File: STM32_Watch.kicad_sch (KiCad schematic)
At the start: 44 parts, among them SW1 SW_Push, SW2 SW_Push, U1 STM32L031K6Ux, U2 LSM6DS3, X1 32.768k

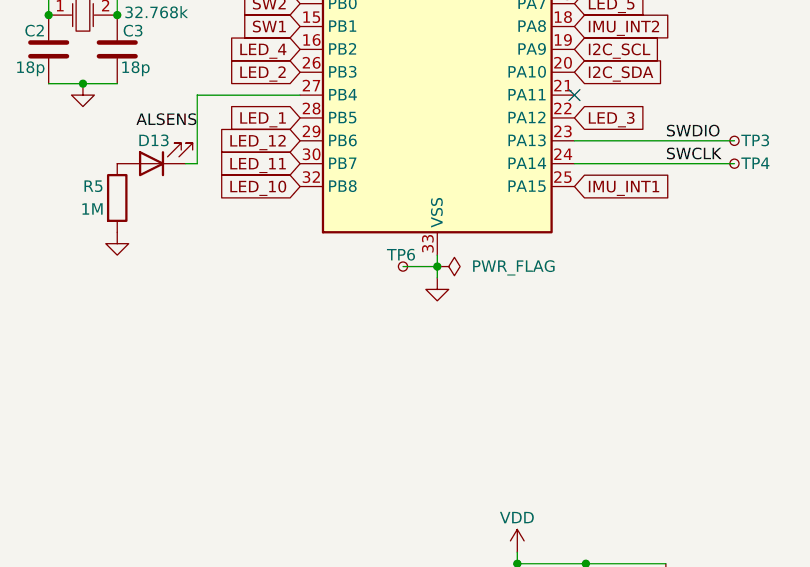
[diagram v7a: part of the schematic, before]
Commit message: Added GND TP & BOM file
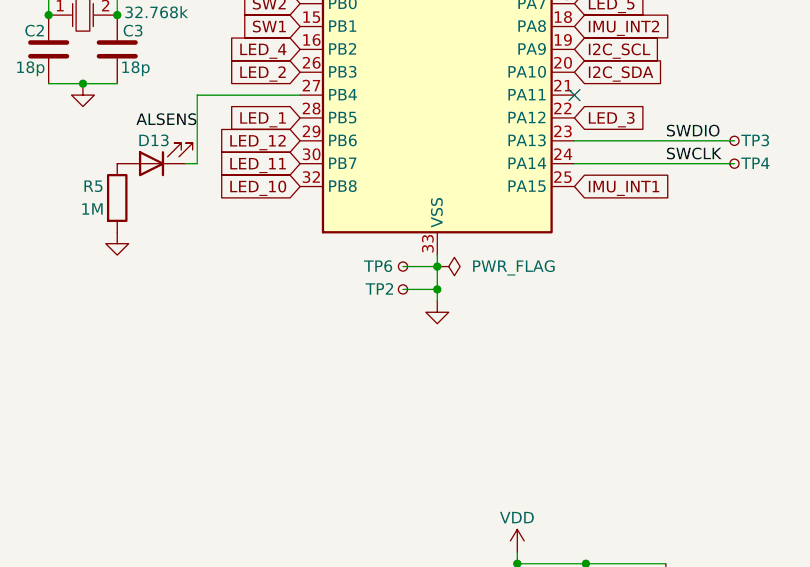
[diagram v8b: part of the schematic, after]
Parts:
- added TP2: TestPoint_Small, TestPoint:TestPoint_Pad_D1.5mm, symbol Connector:TestPoint_Small
- C7: LCSC C15850 -> C32635
- U2: LCSC C967633 -> C94048
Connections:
- net GND: now also TP2.1
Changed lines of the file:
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@@
 	)
 	(junction
+		(at 92.71 102.87)
+		(diameter 0)
+		(color 0 0 0 0)
+	)
+	(junction
 		(at 92.71 34.29)
 		(diameter 0)
@@
 	(wire
 		(pts
-			(xy 92.71 101.6) (xy 92.71 100.33)
+			(xy 88.9 102.87) (xy 92.71 102.87)
+		)
+		(stroke
+			(width 0)
+			(type default)
+		)
+	)
+	(wire
+		(pts
+			(xy 92.71 104.14) (xy 92.71 102.87)
 		)
 		(stroke
@@
 	(wire
 		(pts
+			(xy 92.71 102.87) (xy 92.71 100.33)
+		)
+		(stroke
+			(width 0)
+			(type default)
+		)
+	)
+	(wire
+		(pts
 			(xy 59.69 162.56) (xy 86.36 162.56)
 		)
@@
 	(symbol
 		(lib_id "power:GND")
-		(at 92.71 101.6 0)
+		(at 92.71 104.14 0)
 		(unit 1)
 		(exclude_from_sim no)
@@
 		(fields_autoplaced yes)
 		(property "Reference" "#PWR01"
-			(at 92.71 107.95 0)
+			(at 92.71 110.49 0)
 			(effects
 				(font
@@
 		)
 		(property "Value" "GND"
-			(at 92.71 106.68 0)
+			(at 92.71 109.22 0)
 			(effects
 				(font
@@
 		)
 		(property "Footprint" ""
-			(at 92.71 101.6 0)
+			(at 92.71 104.14 0)
 			(effects
 				(font
@@
 		)
 		(property "Datasheet" ""
-			(at 92.71 101.6 0)
+			(at 92.71 104.14 0)
 			(effects
 				(font
@@
 		)
 		(property "Description" "Power symbol creates a global label with name \"GND\" , ground"
-			(at 92.71 101.6 0)
+			(at 92.71 104.14 0)
 			(effects
 				(font
@@
 	)
 	(symbol
+		(lib_id "Connector:TestPoint_Small")
+		(at 88.9 102.87 90)
+		(unit 1)
+		(exclude_from_sim no)
+		(in_bom yes)
+		(on_board yes)
+		(dnp no)
+		(property "Reference" "TP2"
+			(at 86.36 102.87 90)
+			(effects
+				(font
+					(size 1.27 1.27)
+				)
+			)
+		)
+		(property "Value" "TestPoint_Small"
+			(at 88.9 100.33 90)
+			(effects
+				(font
+					(size 1.27 1.27)
+				)
+				(hide yes)
+			)
+		)
+		(property "Footprint" "TestPoint:TestPoint_Pad_D1.5mm"
+			(at 88.9 97.79 0)
+			(effects
+				(font
+					(size 1.27 1.27)
+				)
+				(hide yes)
+			)
+		)
+		(property "Datasheet" "~"
+			(at 88.9 97.79 0)
+			(effects
+				(font
+					(size 1.27 1.27)
+				)
+				(hide yes)
+			)
+		)
+		(property "Description" "test point"
+			(at 88.9 102.87 0)
+			(effects
+				(font
+					(size 1.27 1.27)
+				)
+				(hide yes)
+			)
+		)
+		(pin "1"
+		)
+		(instances
+			(project ""
+				(path "/1b502511-4b9c-43d1-bc6f-3ad66e0f6a7c"
+					(reference "TP2")
+					(unit 1)
+				)
+			)
+		)
+	)
+	(symbol
 		(lib_id "Mechanical:MountingHole")
 		(at 144.78 147.32 0)
@@
 			)
 		)
-		(property "LCSC" "C15850"
+		(property "LCSC" "C32635"
 			(at 66.04 38.1 0)
 			(effects
@@
 			)
 		)
-		(property "LCSC" "C967633"
+		(property "LCSC" "C94048"
 			(at 101.6 157.48 0)
 			(effects
@@
 		(dnp no)
 		(property "Reference" "TP6"
-			(at 87.122 99.06 0)
+			(at 84.582 100.33 0)
 			(effects
 				(font
